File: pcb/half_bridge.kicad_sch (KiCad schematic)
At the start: 23 parts, among them U4 IKW40N120H3, U5 IKW40N120H3, U6 UCC21550BDW, U7 SS14

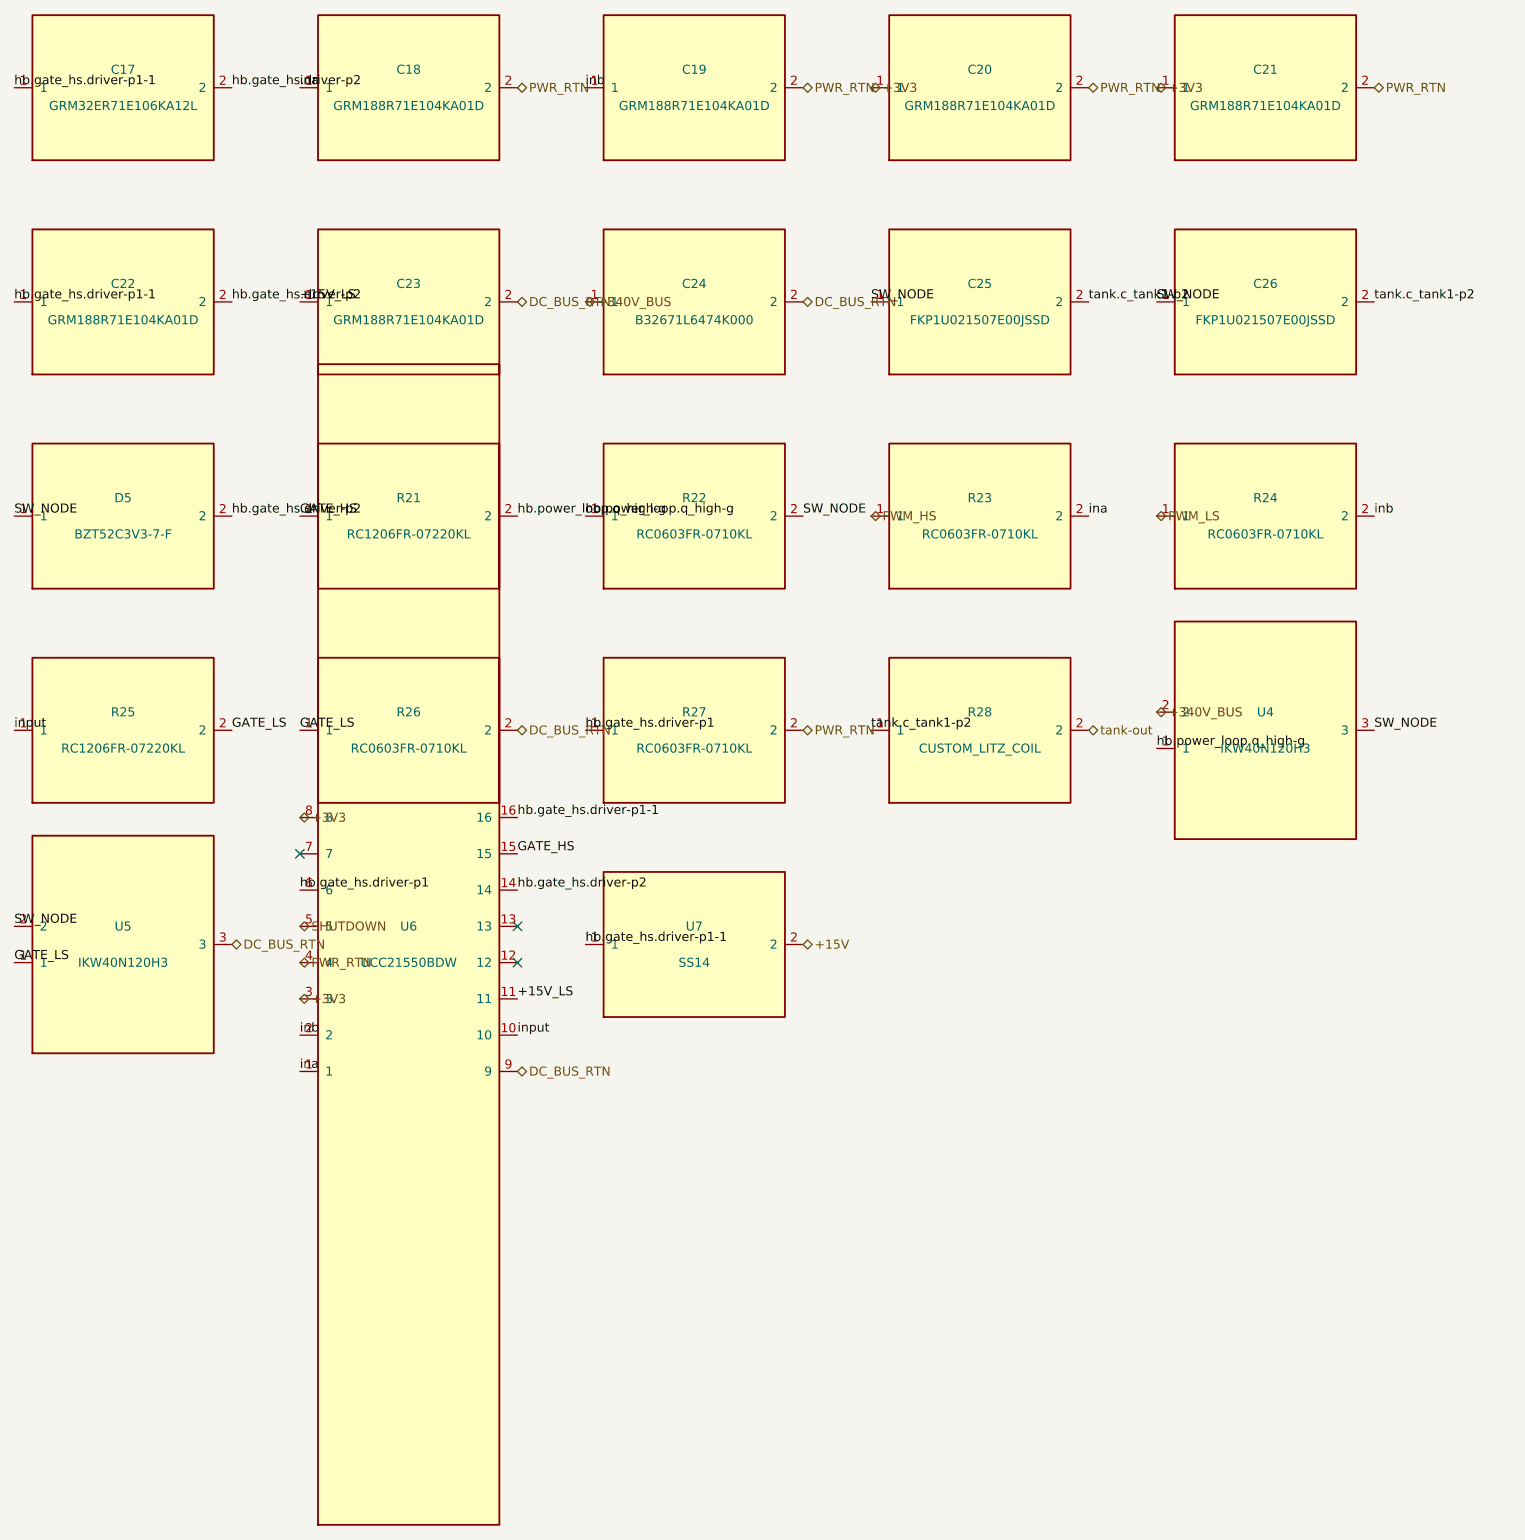
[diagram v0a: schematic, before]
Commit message: fix: board outline placeholder, ten dead CI gates, and the measurement discipline to catch them (#344)
* fix(router): generalize forced-segment fail-closed gate to every net class

_allow_forced_segments() previously only failed closed for HV/AC-class
nets (R6 of the property-test-hardening plan). Every other net --
including congested power/ground nets like vcc, +3V3, PWR_RTN -- still
fell back to a raw, zero-clearance forced segment when the plain A*
pathfinder couldn't find a legal path, which is why shorting_items
didn't improve after the netclass-clearance wiring fix landed.

The gate now disallows forced segments unconditionally, for every net
class, tree-route context, and design_rules state -- reusing the
existing failed_nets/RoutingFailureReport interception plumbing in
attempt_route(), which was already net-class-agnostic.

Also fixes two pre-existing test gaps discovered along the way:
TestHVACForcedSegmentFailClosed's HV/AC tests used net names
(SW_NODE, AC_L) that are themselves excluded from A* by
_should_route()'s pattern matching, so they never actually exercised
the gate -- new tests use non-excluded names that carry the same
safety classification via design_rules instead. And
test_signal_net_still_allows_forced_segments asserted the exact
opposite of the new uniform behavior; flipped and renamed.

See docs/plans/2026-07-24-001-fix-forced-segment-fail-closed-plan.md
(U1, U2).

* test(router): property-test coverage for uniform forced-segment fail-closed

Sweeps every configured net class (plus unclassified) against grids
guaranteed unroutable by construction, proving no forced segment ever
survives and every such net is honestly reported failed. Fails red
against the pre-generalization gate, passes green after -- confirmed
both ways.

Adds unroutable_wall_grids() to astar_property_strategies.py: unlike
grids()'s Bernoulli obstacle density (which may or may not leave a
path open), this guarantees genuine unroutability via a full-height
wall, needed t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
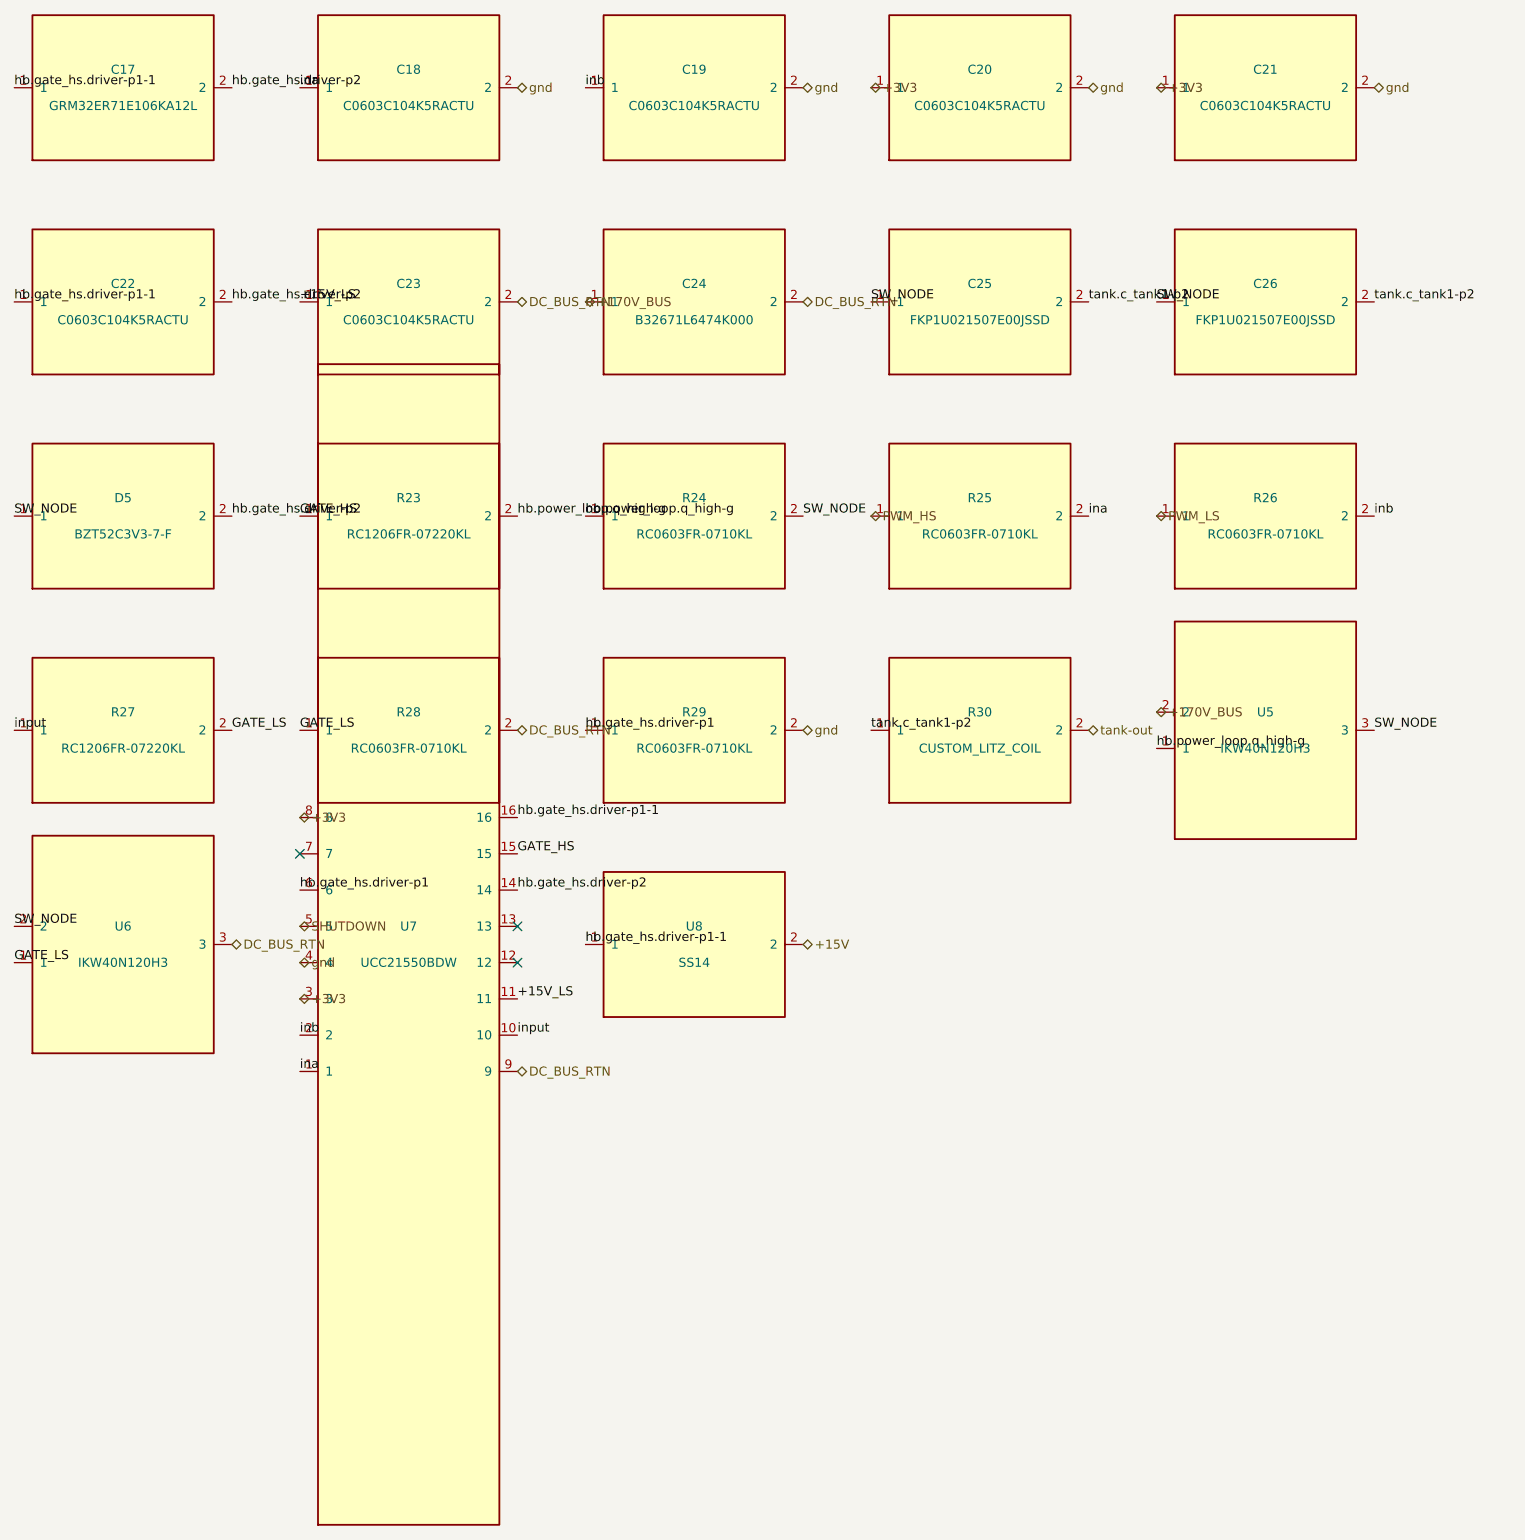
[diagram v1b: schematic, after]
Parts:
- C18, C19, C20, C21, C22, C23: value GRM188R71E104KA01D -> C0603C104K5RACTU; symbol GRM188R71E104KA01D -> C0603C104K5RACTU
- renumbered R21 to R23, R22 to R24, R23 to R25, R24 to R26, R25 to R27, R26 to R28, R27 to R29, R28 to R30, U4 to U5, U5 to U6, U6 to U7, U7 to U8
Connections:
- net +340V_BUS renamed +170V_BUS
- net PWR_RTN renamed gnd
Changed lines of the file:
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@@
   )
   (symbol
-    (lib_id "GRM188R71E104KA01D")
+    (lib_id "C0603C104K5RACTU")
     (at 90.80 50.80 0)
     (unit 1)
@@
     (dnp no)
     (property "Reference" "C18" (at 90.80 48.26 0) (effects (font (size 1.27 1.27))))
-    (property "Value" "GRM188R71E104KA01D" (at 90.80 53.34 0) (effects (font (size 1.27 1.27))))
+    (property "Value" "C0603C104K5RACTU" (at 90.80 53.34 0) (effects (font (size 1.27 1.27))))
     (property "Footprint" "Capacitor_SMD:C_0603_1608Metric" (at 90.80 50.80 0) (effects (font (size 1.27 1.27)) hide))
     (pin "1")
@@
     (effects (font (size 1.27 1.27)) (justify left bottom))
   )
-  (hierarchical_label "PWR_RTN"
+  (hierarchical_label "gnd"
     (shape bidirectional)
     (at 106.04 50.80 0)
@@
   )
   (symbol
-    (lib_id "GRM188R71E104KA01D")
+    (lib_id "C0603C104K5RACTU")
     (at 130.80 50.80 0)
     (unit 1)
@@
     (dnp no)
     (property "Reference" "C19" (at 130.80 48.26 0) (effects (font (size 1.27 1.27))))
-    (property "Value" "GRM188R71E104KA01D" (at 130.80 53.34 0) (effects (font (size 1.27 1.27))))
+    (property "Value" "C0603C104K5RACTU" (at 130.80 53.34 0) (effects (font (size 1.27 1.27))))
     (property "Footprint" "Capacitor_SMD:C_0603_1608Metric" (at 130.80 50.80 0) (effects (font (size 1.27 1.27)) hide))
     (pin "1")
@@
     (effects (font (size 1.27 1.27)) (justify left bottom))
   )
-  (hierarchical_label "PWR_RTN"
+  (hierarchical_label "gnd"
     (shape bidirectional)
     (at 146.04 50.80 0)
@@
   )
   (symbol
-    (lib_id "GRM188R71E104KA01D")
+    (lib_id "C0603C104K5RACTU")
     (at 170.80 50.80 0)
     (unit 1)
@@
     (dnp no)
     (property "Reference" "C20" (at 170.80 48.26 0) (effects (font (size 1.27 1.27))))
-    (property "Value" "GRM188R71E104KA01D" (at 170.80 53.34 0) (effects (font (size 1.27 1.27))))
+    (property "Value" "C0603C104K5RACTU" (at 170.80 53.34 0) (effects (font (size 1.27 1.27))))
     (property "Footprint" "Capacitor_SMD:C_0603_1608Metric" (at 170.80 50.80 0) (effects (font (size 1.27 1.27)) hide))
     (pin "1")
@@
     (effects (font (size 1.27 1.27)) (justify left bottom))
   )
-  (hierarchical_label "PWR_RTN"
+  (hierarchical_label "gnd"
     (shape bidirectional)
     (at 186.04 50.80 0)
@@
   )
   (symbol
-    (lib_id "GRM188R71E104KA01D")
+    (lib_id "C0603C104K5RACTU")
     (at 210.80 50.80 0)
     (unit 1)
@@
     (dnp no)
     (property "Reference" "C21" (at 210.80 48.26 0) (effects (font (size 1.27 1.27))))
-    (property "Value" "GRM188R71E104KA01D" (at 210.80 53.34 0) (effects (font (size 1.27 1.27))))
+    (property "Value" "C0603C104K5RACTU" (at 210.80 53.34 0) (effects (font (size 1.27 1.27))))
     (property "Footprint" "Capacitor_SMD:C_0603_1608Metric" (at 210.80 50.80 0) (effects (font (size 1.27 1.27)) hide))
     (pin "1")
@@
     (effects (font (size 1.27 1.27)) (justify left bottom))
   )
-  (hierarchical_label "PWR_RTN"
+  (hierarchical_label "gnd"
     (shape bidirectional)
     (at 226.04 50.80 0)
@@
   )
   (symbol
-    (lib_id "GRM188R71E104KA01D")
+    (lib_id "C0603C104K5RACTU")
     (at 50.80 80.80 0)
     (unit 1)
@@
     (dnp no)
     (property "Reference" "C22" (at 50.80 78.26 0) (effects (font (size 1.27 1.27))))
-    (property "Value" "GRM188R71E104KA01D" (at 50.80 83.34 0) (effects (font (size 1.27 1.27))))
+    (property "Value" "C0603C104K5RACTU" (at 50.80 83.34 0) (effects (font (size 1.27 1.27))))
     (property "Footprint" "Capacitor_SMD:C_0603_1608Metric" (at 50.80 80.80 0) (effects (font (size 1.27 1.27)) hide))
     (pin "1")
@@
   )
   (symbol
-    (lib_id "GRM188R71E104KA01D")
+    (lib_id "C0603C104K5RACTU")
     (at 90.80 80.80 0)
     (unit 1)
@@
     (dnp no)
     (property "Reference" "C23" (at 90.80 78.26 0) (effects (font (size 1.27 1.27))))
-    (property "Value" "GRM188R71E104KA01D" (at 90.80 83.34 0) (effects (font (size 1.27 1.27))))
+    (property "Value" "C0603C104K5RACTU" (at 90.80 83.34 0) (effects (font (size 1.27 1.27))))
     (property "Footprint" "Capacitor_SMD:C_0603_1608Metric" (at 90.80 80.80 0) (effects (font (size 1.27 1.27)) hide))
     (pin "1")
@@
     (pin "2")
   )
-  (hierarchical_label "+340V_BUS"
+  (hierarchical_label "+170V_BUS"
     (shape bidirectional)
     (at 115.56 80.80 0)
@@
     (on_board yes)
     (dnp no)
-    (property "Reference" "R21" (at 90.80 108.26 0) (effects (font (size 1.27 1.27))))
+    (property "Reference" "R23" (at 90.80 108.26 0) (effects (font (size 1.27 1.27))))
     (property "Value" "RC1206FR-07220KL" (at 90.80 113.34 0) (effects (font (size 1.27 1.27))))
     (property "Footprint" "Resistor_SMD:R_1206_3216Metric" (at 90.80 110.80 0) (effects (font (size 1.27 1.27)) hide))
@@
     (on_board yes)
     (dnp no)
-    (property "Reference" "R22" (at 130.80 108.26 0) (effects (font (size 1.27 1.27))))
+    (property "Reference" "R24" (at 130.80 108.26 0) (effects (font (size 1.27 1.27))))
     (property "Value" "RC0603FR-0710KL" (at 130.80 113.34 0) (effects (font (size 1.27 1.27))))
     (property "Footprint" "Resistor_SMD:R_0603_1608Metric" (at 130.80 110.80 0) (effects (font (size 1.27 1.27)) hide))
@@
     (on_board yes)
     (dnp no)
-    (property "Reference" "R23" (at 170.80 108.26 0) (effects (font (size 1.27 1.27))))
+    (property "Reference" "R25" (at 170.80 108.26 0) (effects (font (size 1.27 1.27))))
     (property "Value" "RC0603FR-0710KL" (at 170.80 113.34 0) (effects (font (size 1.27 1.27))))
     (property "Footprint" "Resistor_SMD:R_0603_1608Metric" (at 170.80 110.80 0) (effects (font (size 1.27 1.27)) hide))
@@
     (on_board yes)
     (dnp no)
-    (property "Reference" "R24" (at 210.80 108.26 0) (effects (font (size 1.27 1.27))))
+    (property "Reference" "R26" (at 210.80 108.26 0) (effects (font (size 1.27 1.27))))
     (property "Value" "RC0603FR-0710KL" (at 210.80 113.34 0) (effects (font (size 1.27 1.27))))
     (property "Footprint" "Resistor_SMD:R_0603_1608Metric" (at 210.80 110.80 0) (effects (font (size 1.27 1.27)) hide))
@@
     (on_board yes)
     (dnp no)
-    (property "Reference" "R25" (at 50.80 138.26 0) (effects (font (size 1.27 1.27))))
+    (property "Reference" "R27" (at 50.80 138.26 0) (effects (font (size 1.27 1.27))))
     (property "Value" "RC1206FR-07220KL" (at 50.80 143.34 0) (effects (font (size 1.27 1.27))))
     (property "Footprint" "Resistor_SMD:R_1206_3216Metric" (at 50.80 140.80 0) (effects (font (size 1.27 1.27)) hide))
@@
     (on_board yes)
     (dnp no)
-    (property "Reference" "R26" (at 90.80 138.26 0) (effects (font (size 1.27 1.27))))
+    (property "Reference" "R28" (at 90.80 138.26 0) (effects (font (size 1.27 1.27))))
     (property "Value" "RC0603FR-0710KL" (at 90.80 143.34 0) (effects (font (size 1.27 1.27))))
     (property "Footprint" "Resistor_SMD:R_0603_1608Metric" (at 90.80 140.80 0) (effects (font (size 1.27 1.27)) hide))
@@
     (on_board yes)
     (dnp no)
-    (property "Reference" "R27" (at 130.80 138.26 0) (effects (font (size 1.27 1.27))))
+    (property "Reference" "R29" (at 130.80 138.26 0) (effects (font (size 1.27 1.27))))
     (property "Value" "RC0603FR-0710KL" (at 130.80 143.34 0) (effects (font (size 1.27 1.27))))
     (property "Footprint" "Resistor_SMD:R_0603_1608Metric" (at 130.80 140.80 0) (effects (font (size 1.27 1.27)) hide))
@@
     (effects (font (size 1.27 1.27)) (justify left bottom))
   )
-  (hierarchical_label "PWR_RTN"
+  (hierarchical_label "gnd"
     (shape bidirectional)
     (at 146.04 140.80 0)
@@
     (on_board yes)
     (dnp no)
-    (property "Reference" "R28" (at 170.80 138.26 0) (effects (font (size 1.27 1.27))))
+    (property "Reference" "R30" (at 170.80 138.26 0) (effects (font (size 1.27 1.27))))
     (property "Value" "CUSTOM_LITZ_COIL" (at 170.80 143.34 0) (effects (font (size 1.27 1.27))))
     (property "Footprint" "lib:LitzPad_15A" (at 170.80 140.80 0) (effects (font (size 1.27 1.27)) hide))
@@
     (on_board yes)
     (dnp no)
-    (property "Reference" "U4" (at 210.80 138.26 0) (effects (font (size 1.27 1.27))))
+    (property "Reference" "U5" (at 210.80 138.26 0) (effects (font (size 1.27 1.27))))
     (property "Value" "IKW40N120H3" (at 210.80 143.34 0) (effects (font (size 1.27 1.27))))
     (property "Footprint" "Package_TO_SOT_THT:TO-247-3_Vertical" (at 210.80 140.80 0) (effects (font (size 1.27 1.27)) hide))
@@
     (effects (font (size 1.27 1.27)) (justify left bottom))
   )
-  (hierarchical_label "+340V_BUS"
+  (hierarchical_label "+170V_BUS"
     (shape bidirectional)
     (at 195.56 138.26 0)
@@
     (on_board yes)
     (dnp no)
-    (property "Reference" "U5" (at 50.80 168.26 0) (effects (font (size 1.27 1.27))))
+    (property "Reference" "U6" (at 50.80 168.26 0) (effects (font (size 1.27 1.27))))
     (property "Value" "IKW40N120H3" (at 50.80 173.34 0) (effects (font (size 1.27 1.27))))
     (property "Footprint" "Package_TO_SOT_THT:TO-247-3_Vertical" (at 50.80 170.80 0) (effects (font (size 1.27 1.27)) hide))
@@
     (on_board yes)
     (dnp no)
-    (property "Reference" "U6" (at 90.80 168.26 0) (effects (font (size 1.27 1.27))))
+    (property "Reference" "U7" (at 90.80 168.26 0) (effects (font (size 1.27 1.27))))
     (property "Value" "UCC21550BDW" (at 90.80 173.34 0) (effects (font (size 1.27 1.27))))
     (property "Footprint" "lib:SOIC16W_Isolated" (at 90.80 170.80 0) (effects (font (size 1.27 1.27)) hide))
@@
     (effects (font (size 1.27 1.27)) (justify left bottom))
   )
-  (hierarchical_label "PWR_RTN"
+  (hierarchical_label "gnd"
     (shape bidirectional)
     (at 75.56 173.34 0)
@@
     (on_board yes)
     (dnp no)
-    (property "Reference" "U7" (at 130.80 168.26 0) (effects (font (size 1.27 1.27))))
+    (property "Reference" "U8" (at 130.80 168.26 0) (effects (font (size 1.27 1.27))))
     (property "Value" "SS14" (at 130.80 173.34 0) (effects (font (size 1.27 1.27))))
     (property "Footprint" "Diode_SMD:D_SMA" (at 130.80 170.80 0) (effects (font (size 1.27 1.27)) hide))
